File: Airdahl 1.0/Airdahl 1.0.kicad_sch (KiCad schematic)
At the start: 18 parts, among them J1 Conn_ARM_JTAG_SWD_20, SW1 SW_MEC_5E, U1 STM32F446RETx, X2 ABS25-32.768KHZ-6-T

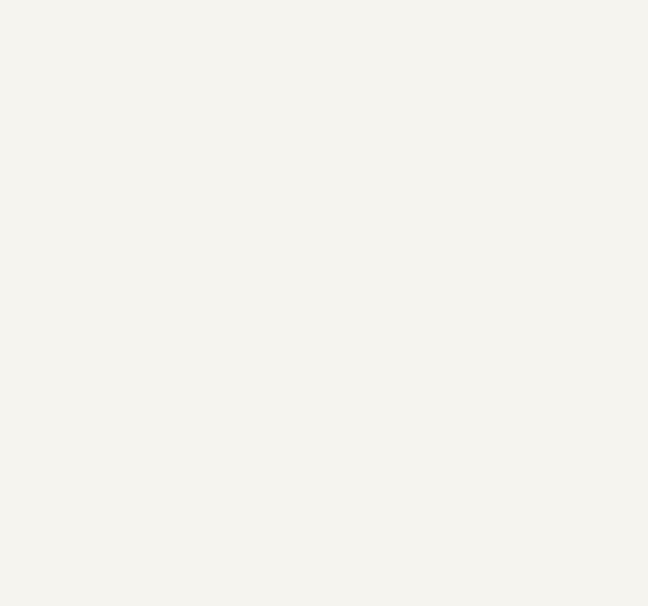
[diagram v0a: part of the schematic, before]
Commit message: buck converter diode array and also pyro channels bc why not
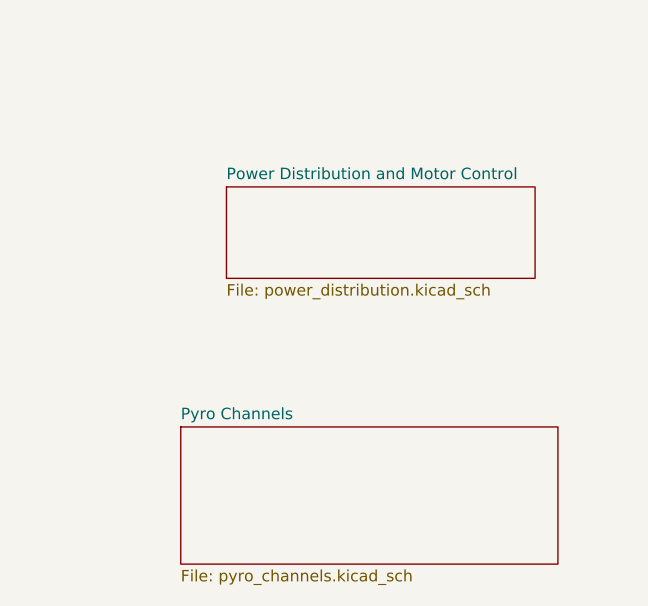
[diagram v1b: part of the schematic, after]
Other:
- added sheet Power Distribution and Motor Control (power_distribution.kicad_sch)
- added sheet Pyro Channels (pyro_channels.kicad_sch)
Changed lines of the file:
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@@
+		)
+	)
+	(sheet
+		(at 245.11 218.44)
+		(size 34.29 10.16)
+		(exclude_from_sim no)
+		(in_bom yes)
+		(on_board yes)
+		(dnp no)
+		(fields_autoplaced yes)
+		(stroke
+			(width 0.1524)
+			(type solid)
+		)
+		(fill
+			(color 0 0 0 0.0000)
+		)
+		(property "Sheetname" "Power Distribution and Motor Control"
+			(at 245.11 217.7284 0)
+			(effects
+				(font
+					(size 1.27 1.27)
+				)
+				(justify left bottom)
+			)
+		)
+		(property "Sheetfile" "power_distribution.kicad_sch"
+			(at 245.11 229.1846 0)
+			(effects
+				(font
+					(size 1.27 1.27)
+				)
+				(justify left top)
+			)
+		)
+		(instances
+			(project "Airdahl 1.0"
+				(path "/e2c992a5-0f37-48ff-88a4-7c40cfcda45e"
+					(page "2")
+				)
+			)
+		)
+	)
+	(sheet
+		(at 240.03 245.11)
+		(size 41.91 15.24)
+		(exclude_from_sim no)
+		(in_bom yes)
+		(on_board yes)
+		(dnp no)
+		(fields_autoplaced yes)
+		(stroke
+			(width 0.1524)
+			(type solid)
+		)
+		(fill
+			(color 0 0 0 0.0000)
+		)
+		(property "Sheetname" "Pyro Channels"
+			(at 240.03 244.3984 0)
+			(effects
+				(font
+					(size 1.27 1.27)
+				)
+				(justify left bottom)
+			)
+		)
+		(property "Sheetfile" "pyro_channels.kicad_sch"
+			(at 240.03 260.9346 0)
+			(effects
+				(font
+					(size 1.27 1.27)
+				)
+				(justify left top)
+			)
+		)
+		(instances
+			(project "Airdahl 1.0"
+				(path "/e2c992a5-0f37-48ff-88a4-7c40cfcda45e"
+					(page "3")
+				)
+			)
 		)
 	)

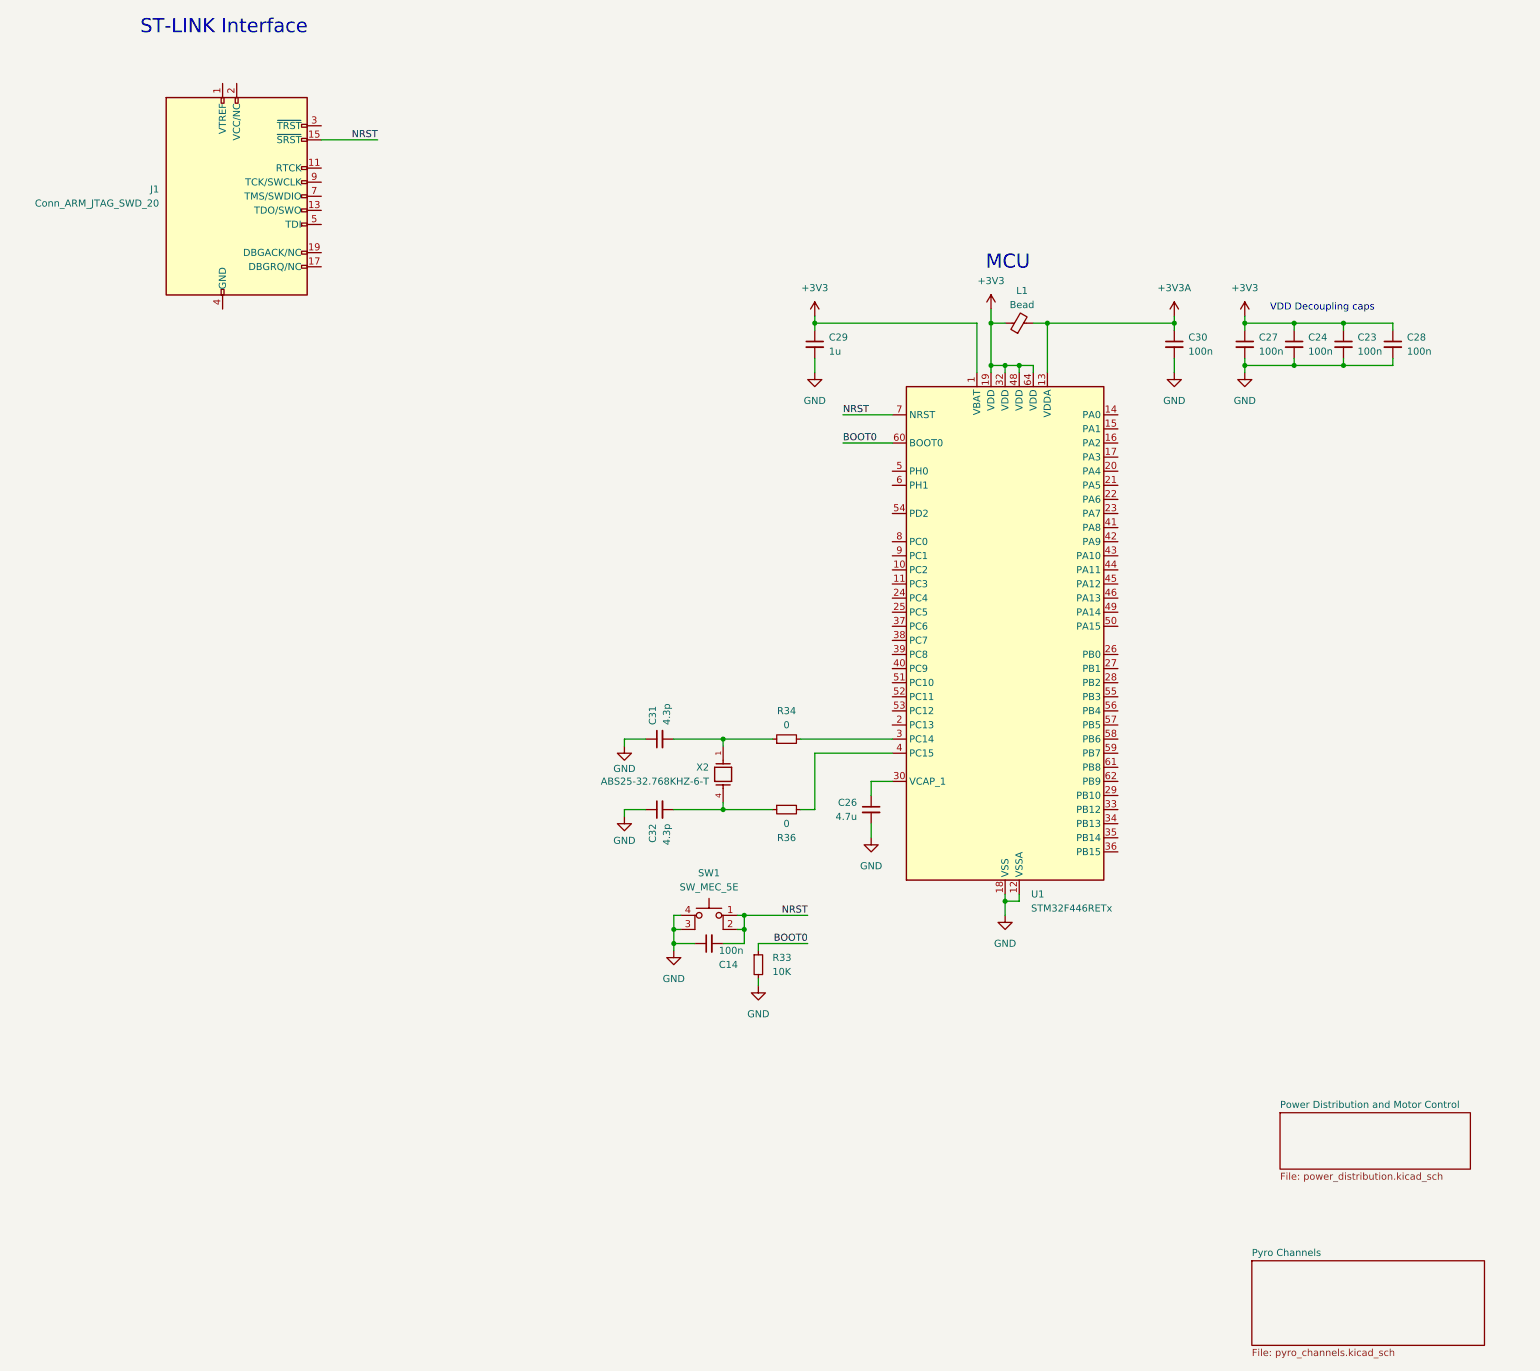
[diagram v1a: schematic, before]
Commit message: HSE crystal + gaslit st-link into powering board
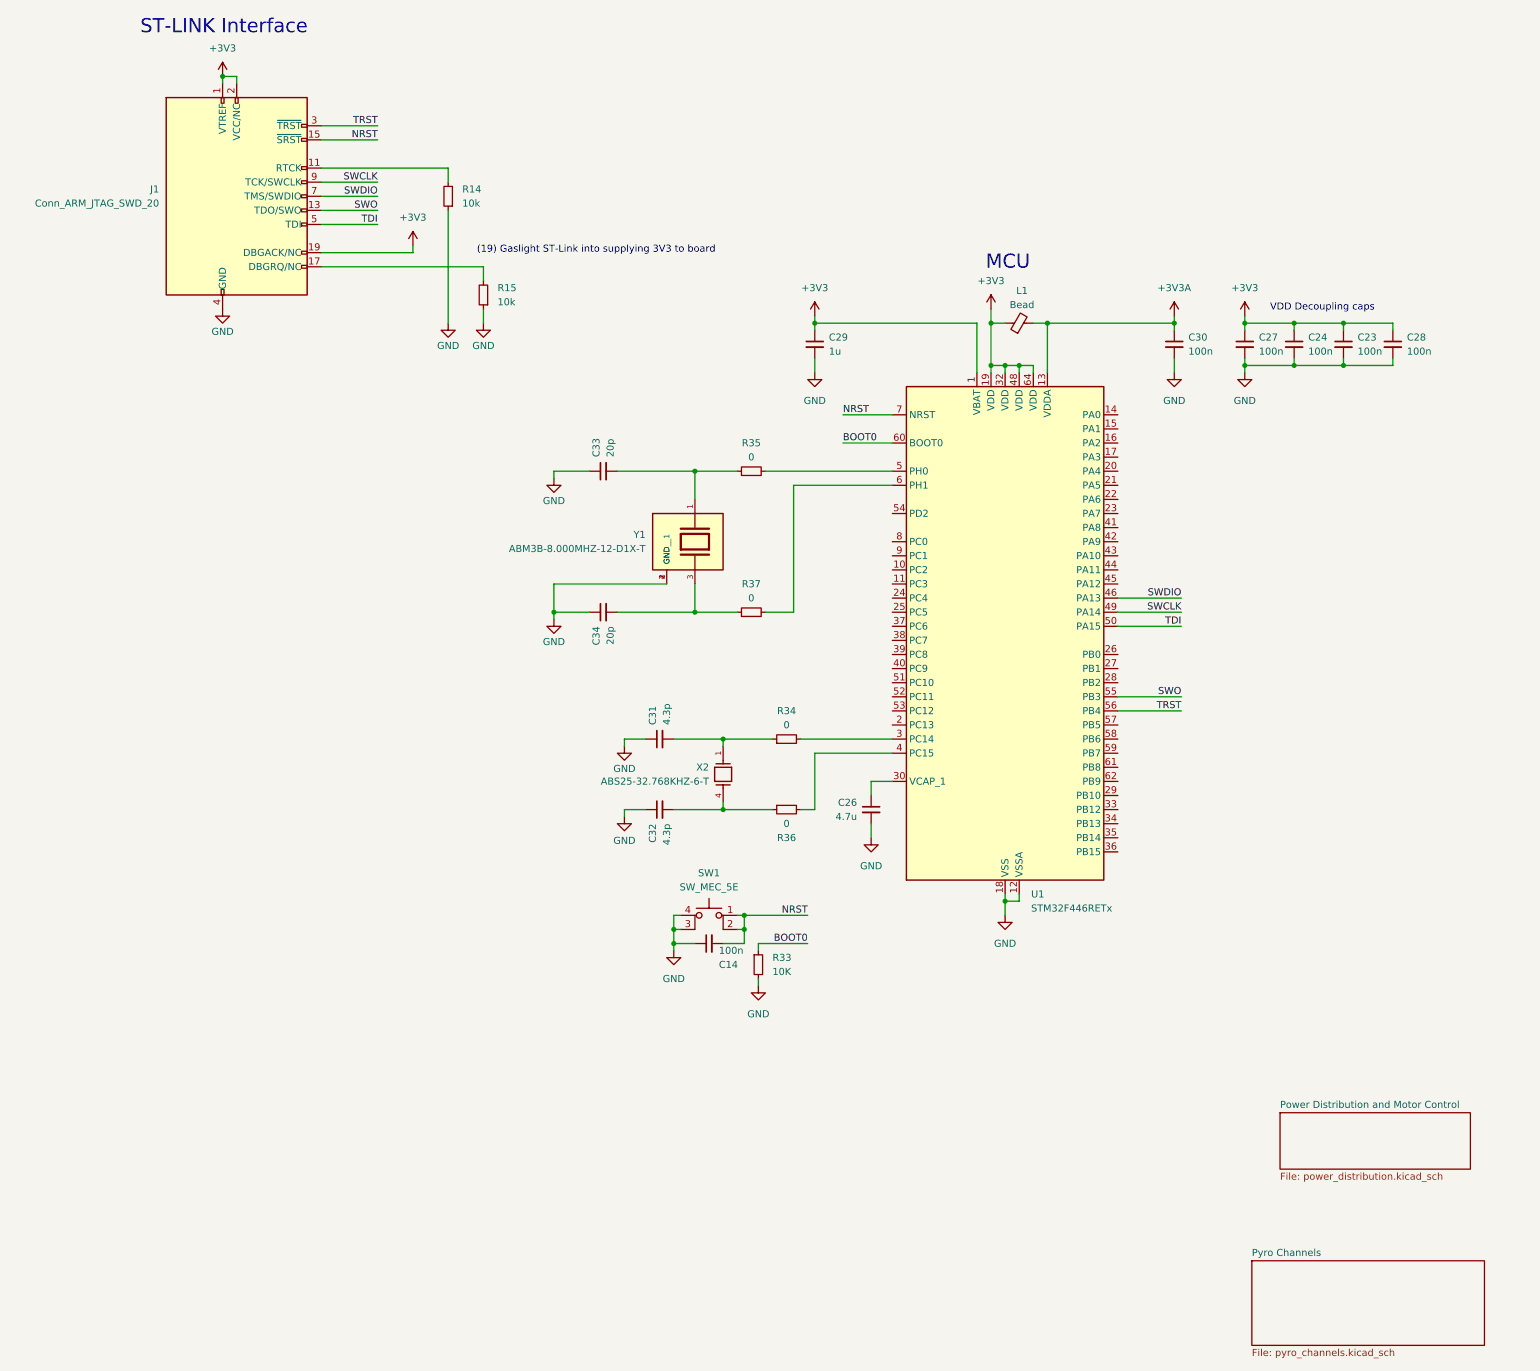
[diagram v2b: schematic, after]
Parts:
- added C33, C34: 20p, Capacitor_SMD:C_0603_1608Metric_Pad1.08x0.95mm_HandSolder, symbol Device:C_Small
- added R14, R15: 10k, Resistor_SMD:R_0201_0603Metric_Pad0.64x0.40mm_HandSolder, symbol Device:R_Small
- added R35, R37: 0, Resistor_SMD:R_0201_0603Metric_Pad0.64x0.40mm_HandSolder, symbol Device:R_Small
- added Y1: ABM3B-8.000MHZ-12-D1X-T, ABM3B-8.000MHZ-12-D1X-T:XTAL_ABM3B-8.000MHZ-12-D1X-T, symbol ABM3B-8.000MHZ-12-D1X-T:ABM3B-8.000MHZ-12-D1X-T
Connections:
- net +3V3: now also J1.1 (VTREF), J1.19 (DBGACK/NC), J1.2 (VCC/NC)
- net GND: now also J1.10 (GND), J1.12 (GND), J1.14 (GND), J1.16 (GND), J1.18 (GND), J1.20 (GND), J1.4 (GND), J1.6 (GND), J1.8 (GND), C33.1, C34.1, R14.1, R15.1, Y1.2 (GND), Y1.4 (GND__1)
- net at J1.11 (RTCK): now also R14.2
- net SWO: now reaches J1.13 (TDO/SWO)
- net SWO: now also U1.55 (PB3)
- net at J1.17 (DBGRQ/NC): now also R15.2
- net TRST: now reaches J1.3 (~{TRST})
- net TRST: now also U1.56 (PB4)
- net TDI: now reaches J1.5 (TDI)
- net TDI: now also U1.50 (PA15)
- net SWDIO: now reaches J1.7 (TMS/SWDIO)
- net SWDIO: now also U1.46 (PA13)
- net SWCLK: now reaches J1.9 (TCK/SWCLK)
- net SWCLK: now also U1.49 (PA14)
- net at U1.5 (PH0): now also R35.2
- net at U1.6 (PH1): now also R37.2
- new net: C33.2, R35.1, Y1.1
- new net: C34.2, R37.1, Y1.3
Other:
- note added: "(19) Gaslight ST-Link into supplying 3V3 to board"

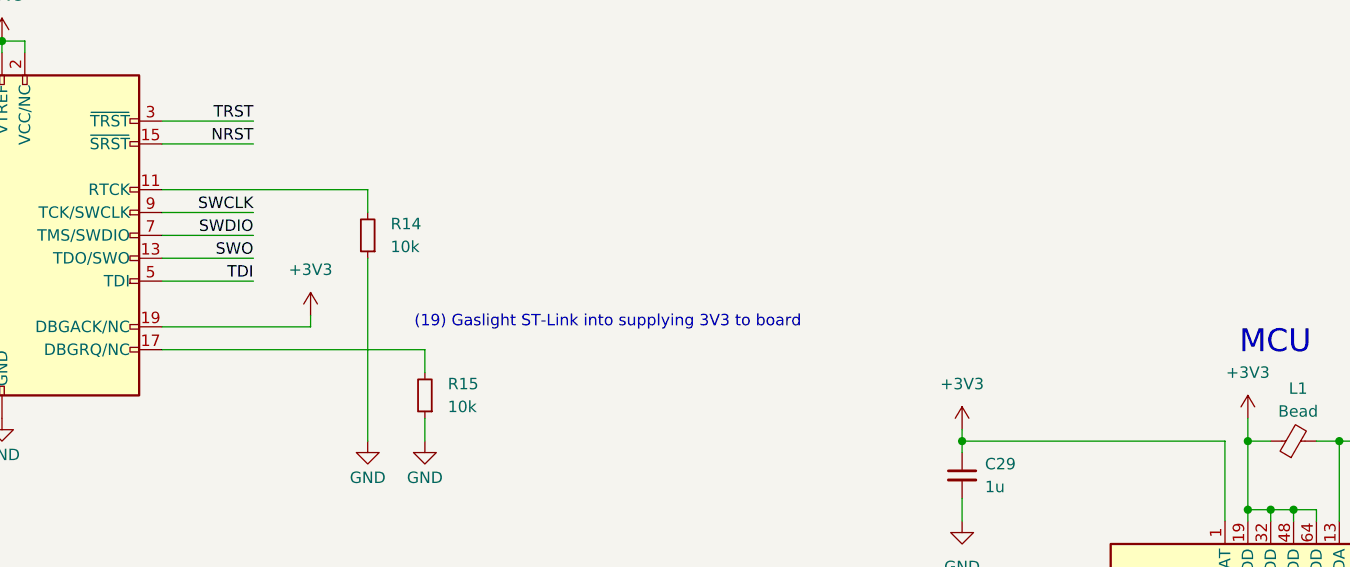
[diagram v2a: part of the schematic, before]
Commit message: switched out buck converter, added OR-ing between stlink and buck
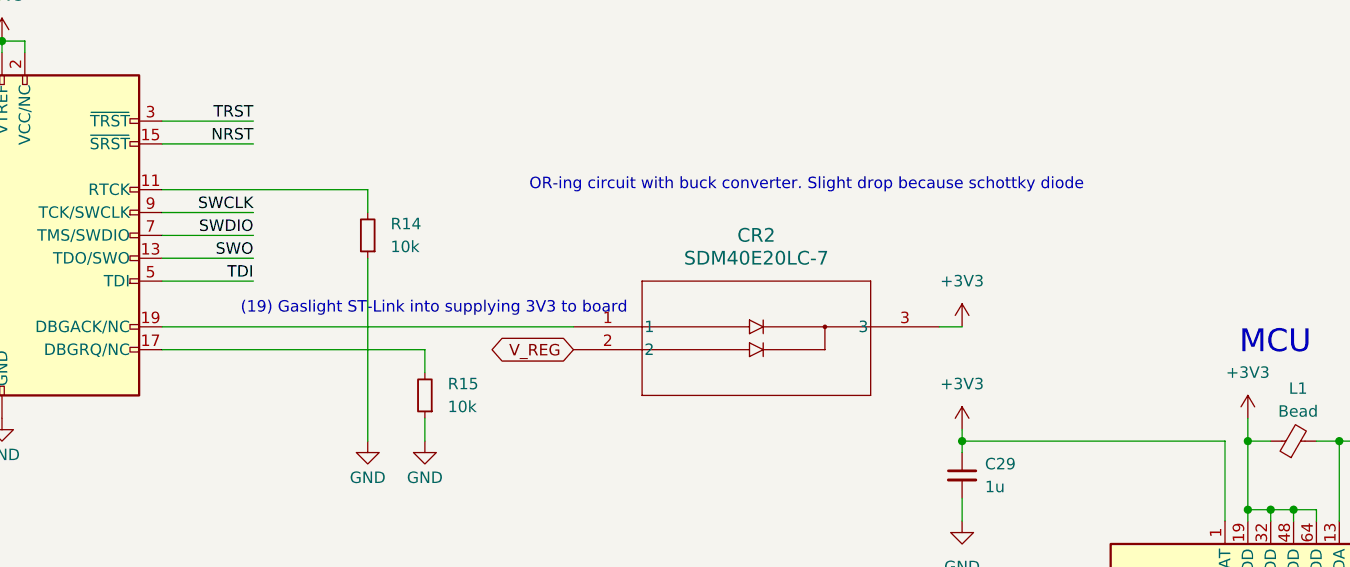
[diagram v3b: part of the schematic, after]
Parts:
- added CR2: SDM40E20LC-7, SOT-23_DIO, symbol SDM40E20LC_7:SDM40E20LC-7
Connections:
- net +3V3: now also CR2.3; no longer J1.19 (DBGACK/NC)
- new net: CR2.1, J1.19 (DBGACK/NC)
- new net V_REG: CR2.2
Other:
- note added: "OR-ing circuit with buck converter. Slight drop because schottky diode"
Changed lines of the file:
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@@
 	(text "(19) Gaslight ST-Link into supplying 3V3 to board"
 		(exclude_from_sim no)
-		(at 121.92 62.992 0)
+		(at 102.616 61.468 0)
 		(effects
 			(font
@@
 		)
 	)
+	(text "OR-ing circuit with buck converter. Slight drop because schottky diode"
+		(exclude_from_sim no)
+		(at 144.018 47.752 0)
+		(effects
+			(font
+				(size 1.27 1.27)
+			)
+		)
+	)
 	(text "ST-LINK Interface"
 		(exclude_from_sim no)
@@
 	(wire
 		(pts
-			(xy 88.9 63.5) (xy 72.39 63.5)
+			(xy 72.39 63.5) (xy 118.11 63.5)
 		)
 		(stroke
@@
 	(wire
 		(pts
-			(xy 88.9 62.23) (xy 88.9 63.5)
-		)
-		(stroke
-			(width 0)
-			(type default)
-		)
-	)
-	(wire
-		(pts
 			(xy 203.2 76.2) (xy 226.06 76.2)
 		)
@@
 	(wire
 		(pts
+			(xy 161.29 63.5) (xy 158.75 63.5)
+		)
+		(stroke
+			(width 0)
+			(type default)
+		)
+	)
+	(wire
+		(pts
 			(xy 101.6 73.66) (xy 101.6 76.2)
 		)
@@
 		)
 	)
+	(global_label "V_REG"
+		(shape bidirectional)
+		(at 118.11 66.04 180)
+		(fields_autoplaced yes)
+		(effects
+			(font
+				(size 1.27 1.27)
+			)
+			(justify right)
+		)
+		(property "Intersheetrefs" "${INTERSHEET_REFS}"
+			(at 108.2683 66.04 0)
+			(effects
+				(font
+					(size 1.27 1.27)
+				)
+				(justify right)
+				(hide yes)
+			)
+		)
+	)
+	(symbol
+		(lib_id "SDM40E20LC_7:SDM40E20LC-7")
+		(at 118.11 63.5 0)
+		(unit 1)
+		(exclude_from_sim no)
+		(in_bom yes)
+		(on_board yes)
+		(dnp no)
+		(property "Reference" "CR2"
+			(at 138.43 53.34 0)
+			(effects
+				(font
+					(size 1.524 1.524)
+				)
+			)
+		)
+		(property "Value" "SDM40E20LC-7"
+			(at 138.43 55.88 0)
+			(effects
+				(font
+					(size 1.524 1.524)
+				)
+			)
+		)
+		(property "Footprint" "SOT-23_DIO"
+			(at 118.11 63.5 0)
+			(effects
+				(font
+					(size 1.27 1.27)
+					(italic yes)
+				)
+				(hide yes)
+			)
+		)
+		(property "Datasheet" "SDM40E20LC-7"
+			(at 118.11 63.5 0)
+			(effects
+				(font
+					(size 1.27 1.27)
+					(italic yes)
+				)
+				(hide yes)
+			)
+		)
+		(property "Description" ""
+			(at 118.11 63.5 0)
+			(effects
+				(font
+					(size 1.27 1.27)
+				)
+				(hide yes)
+			)
+		)
+		(pin "3"
+		)
+		(pin "1"
+		)
+		(pin "2"
+		)
+		(instances
+			(project "Airdahl 1.0"
+				(path "/e2c992a5-0f37-48ff-88a4-7c40cfcda45e"
+					(reference "CR2")
+					(unit 1)
+				)
+			)
+		)
+	)
 	(symbol
 		(lib_id "power:GND")
@@
 	)
 	(symbol
-		(lib_id "power:+3V3")
-		(at 88.9 62.23 0)
-		(unit 1)
-		(exclude_from_sim no)
-		(in_bom yes)
-		(on_board yes)
-		(dnp no)
-		(fields_autoplaced yes)
-		(property "Reference" "#PWR031"
-			(at 88.9 66.04 0)
-			(effects
-				(font
-					(size 1.27 1.27)
-				)
-				(hide yes)
-			)
-		)
-		(property "Value" "+3V3"
-			(at 88.9 57.15 0)
-			(effects
-				(font
-					(size 1.27 1.27)
-				)
-			)
-		)
-		(property "Footprint" ""
-			(at 88.9 62.23 0)
-			(effects
-				(font
-					(size 1.27 1.27)
-				)
-				(hide yes)
-			)
-		)
-		(property "Datasheet" ""
-			(at 88.9 62.23 0)
-			(effects
-				(font
-					(size 1.27 1.27)
-				)
-				(hide yes)
-			)
-		)
-		(property "Description" "Power symbol creates a global label with name \"+3V3\""
-			(at 88.9 62.23 0)
-			(effects
-				(font
-					(size 1.27 1.27)
-				)
-				(hide yes)
-			)
-		)
-		(pin "1"
-		)
-		(instances
-			(project "Airdahl 1.0"
-				(path "/e2c992a5-0f37-48ff-88a4-7c40cfcda45e"
-					(reference "#PWR031")
-					(unit 1)
-				)
-			)
-		)
-	)
-	(symbol
 		(lib_id "ABS25-32.768KHZ-6-T:ABS25-32.768KHZ-6-T")
 		(at 144.78 157.48 90)
@@
 					(unit 1)
 				)
+			)
+		)
+	)
+	(symbol
+		(lib_id "power:+3V3")
+		(at 161.29 63.5 0)
+		(unit 1)
+		(exclude_from_sim no)
+		(in_bom yes)
+		(on_board yes)
+		(dnp no)
+		(fields_autoplaced yes)
+		(property "Reference" "#PWR018"
+			(at 161.29 67.31 0)
+			(effects
+				(font
+					(size 1.27 1.27)
+				)
+				(hide yes)
+			)
+		)
+		(property "Value" "+3V3"
+			(at 161.29 58.42 0)
+			(effects
+				(font
+					(size 1.27 1.27)
+				)
+			)
+		)
+		(property "Footprint" ""
+			(at 161.29 63.5 0)
+			(effects
+				(font
+					(size 1.27 1.27)
+				)
+				(hide yes)
+			)
+		)
+		(property "Datasheet" ""
+			(at 161.29 63.5 0)
+			(effects
+				(font
+					(size 1.27 1.27)
+				)
+				(hide yes)
+			)
+		)
+		(property "Description" "Power symbol creates a global label with name \"+3V3\""
+			(at 161.29 63.5 0)
+			(effects
+				(font
+					(size 1.27 1.27)
+				)
+				(hide yes)
+			)
+		)
+		(pin "1"
+		)
+		(instances
+			(project "Airdahl 1.0"
+				(path "/e2c992a5-0f37-48ff-88a4-7c40cfcda45e"
+					(reference "#PWR018")
+					(unit 1)
+				)
